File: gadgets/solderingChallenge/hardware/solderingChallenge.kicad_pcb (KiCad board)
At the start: 2 copper layers, 145 x 39 mm, 46 parts, among them J10 USB_A, J12 USB_A, J2 USB_A, J4 USB_A, J6 USB_A, J8 USB_A, U1 LM555xN, U2 LMC555xM, U3 LMC555xMM, U4 LMC555xMM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

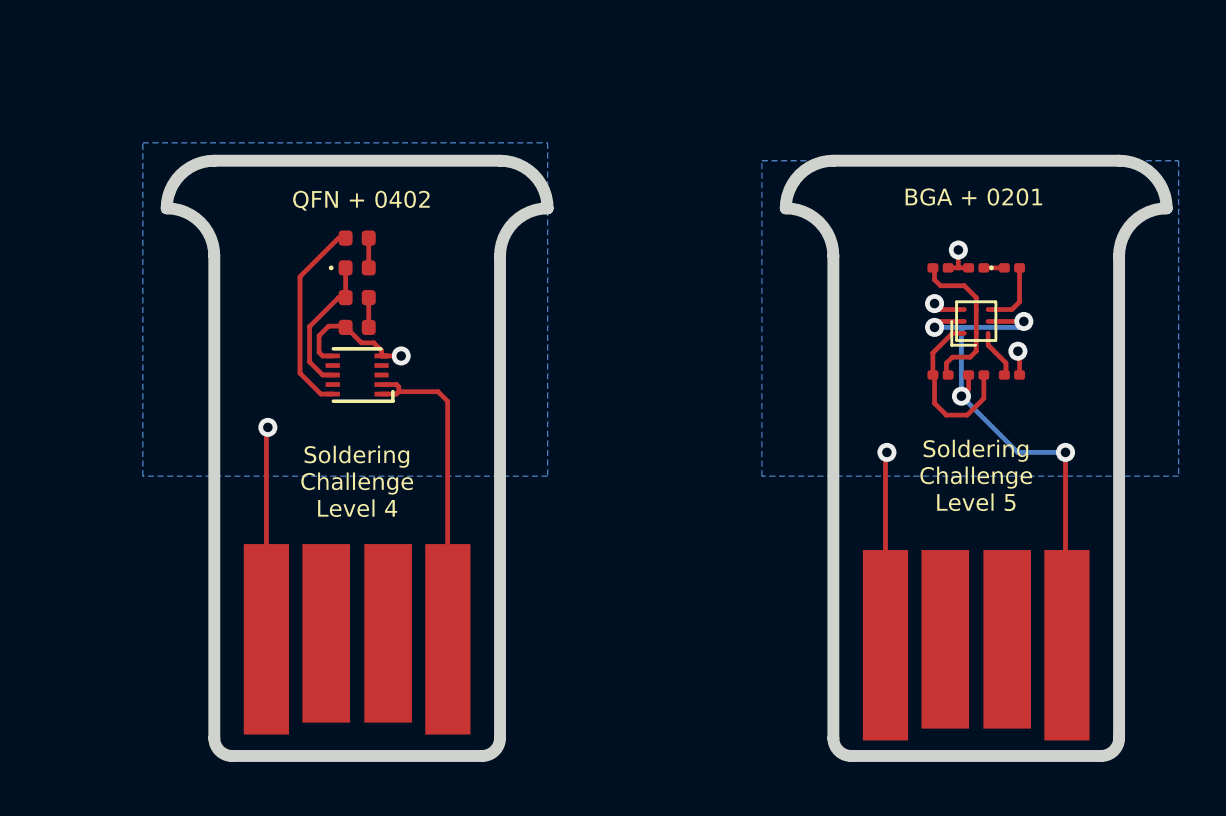
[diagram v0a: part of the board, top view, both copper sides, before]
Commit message: Remove extra level, add documentation
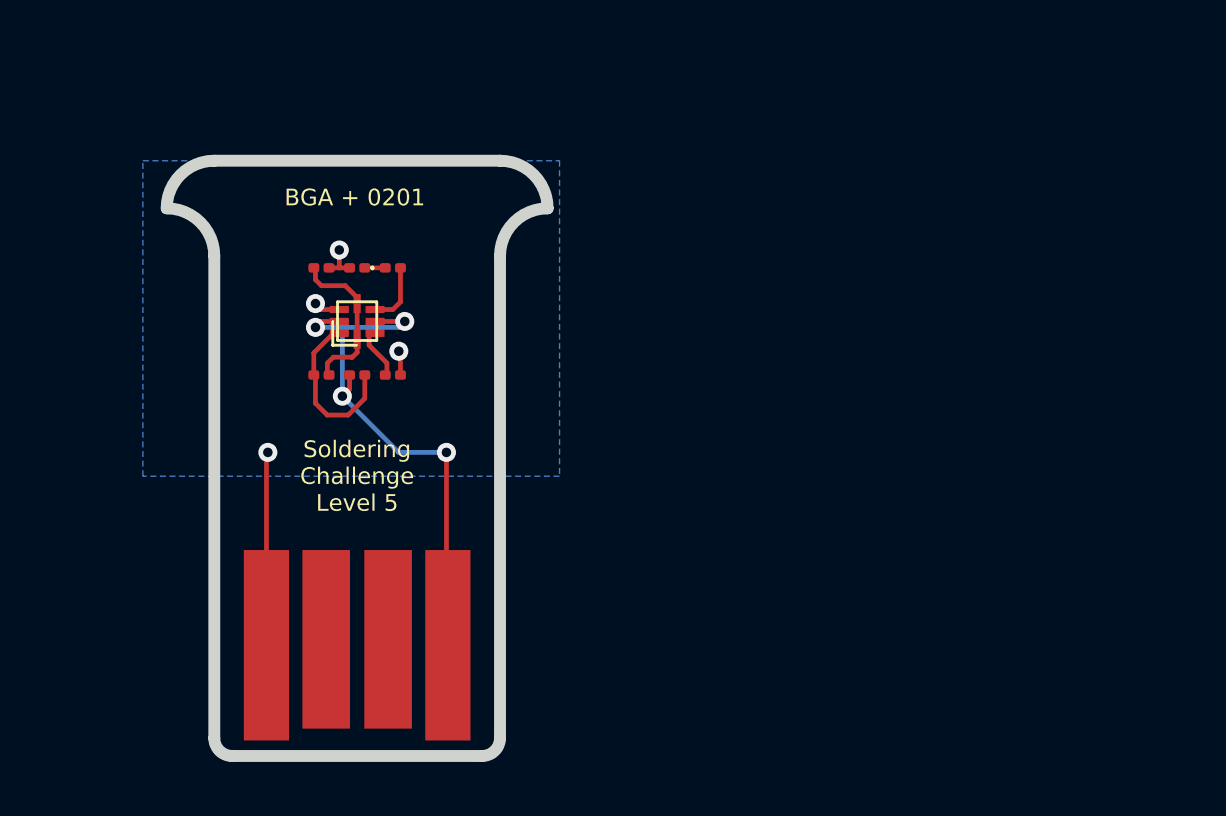
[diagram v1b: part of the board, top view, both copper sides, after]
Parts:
- removed C11: 100n, Capacitor_SMD:C_0402_1005Metric
- removed D6: LED, LED_SMD:LED_0402_1005Metric
- removed J12: USB_A, RoboCamp:usb-PCB
- removed R16: 100k, Resistor_SMD:R_0402_1005Metric
- removed R17: 330R, Resistor_SMD:R_0402_1005Metric
- removed U6: MIC1555-MU, RoboCamp:UTDFN-10
- moved C10 26.0 mm to (190.5, 91.2)
- moved C9 26.0 mm to (193.5, 95.8)
- moved D5 26.0 mm to (193.5, 91.2)
- moved J10 26.0 mm to (192.0, 112.0)
- moved R13 26.0 mm to (192.0, 91.2)
- moved R14 26.0 mm to (192.0, 95.8)
- moved R15 26.0 mm to (190.5, 95.8)
- moved U5 26.0 mm to (192.0, 93.5)
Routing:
- net /Level 4 alternative - 0402/GND: track 14.8 -> 0.00 mm, vias 2 -> 0
- net /Level 4 alternative - 0402/VCC: track 14.0 -> 0.00 mm
- net Net-(R17-Pad2): track 8.38 -> 0.00 mm
- net Net-(C11-Pad2): track 5.98 -> 0.00 mm
- net Net-(D6-Pad2): track 1.21 -> 0.00 mm
- net Net-(C11-Pad1): track 1.21 -> 0.00 mm
- net /Level 5 - 0201/VCC: track 24.3 -> 24.9 mm
- net Net-(C9-Pad1): track 2.06 -> 2.61 mm
- removed copper zone on B.Cu, net /Level 4 alternative - 0402/GND
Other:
- board size 145 x 39 mm -> 119 x 39 mm
- net class Default: clearance 0.2 -> 0.127
- rule trace_clearance: 0.2 -> 0.127
- board text removed: "QFN + 0402"

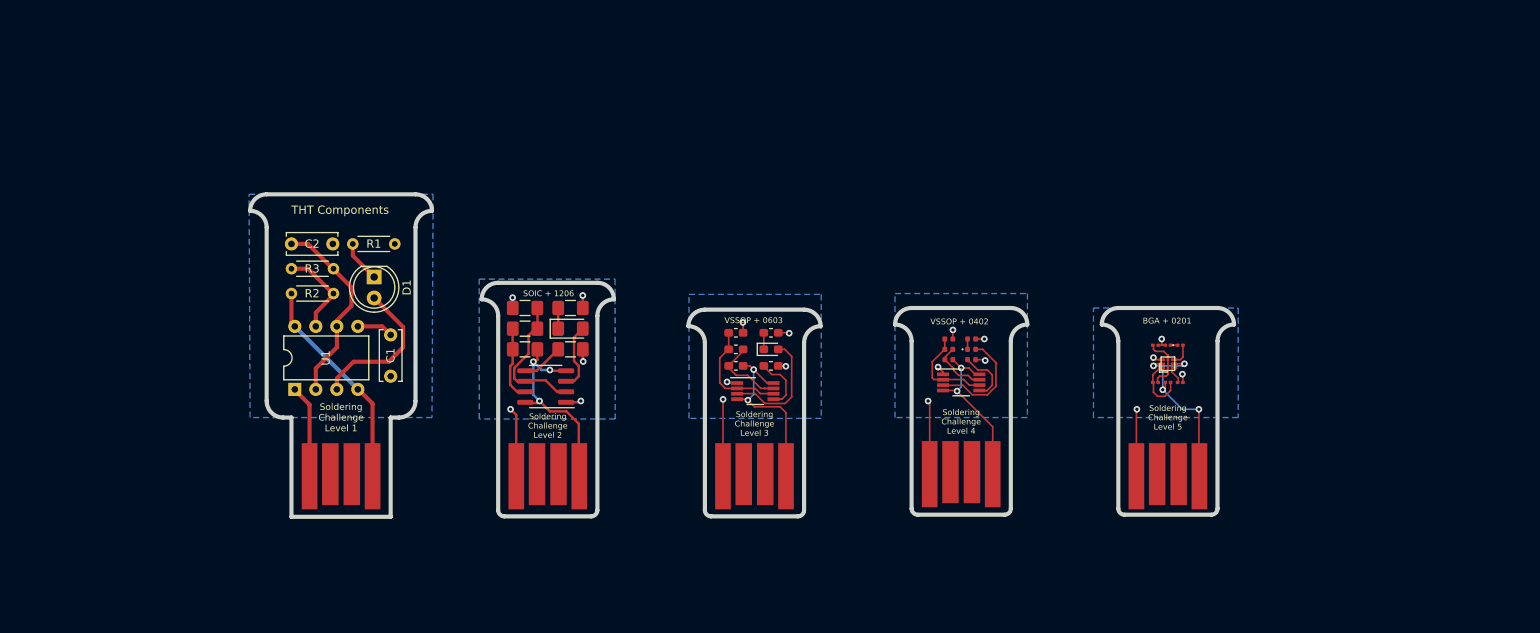
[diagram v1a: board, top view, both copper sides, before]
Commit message: Add L0 to soldering challenge
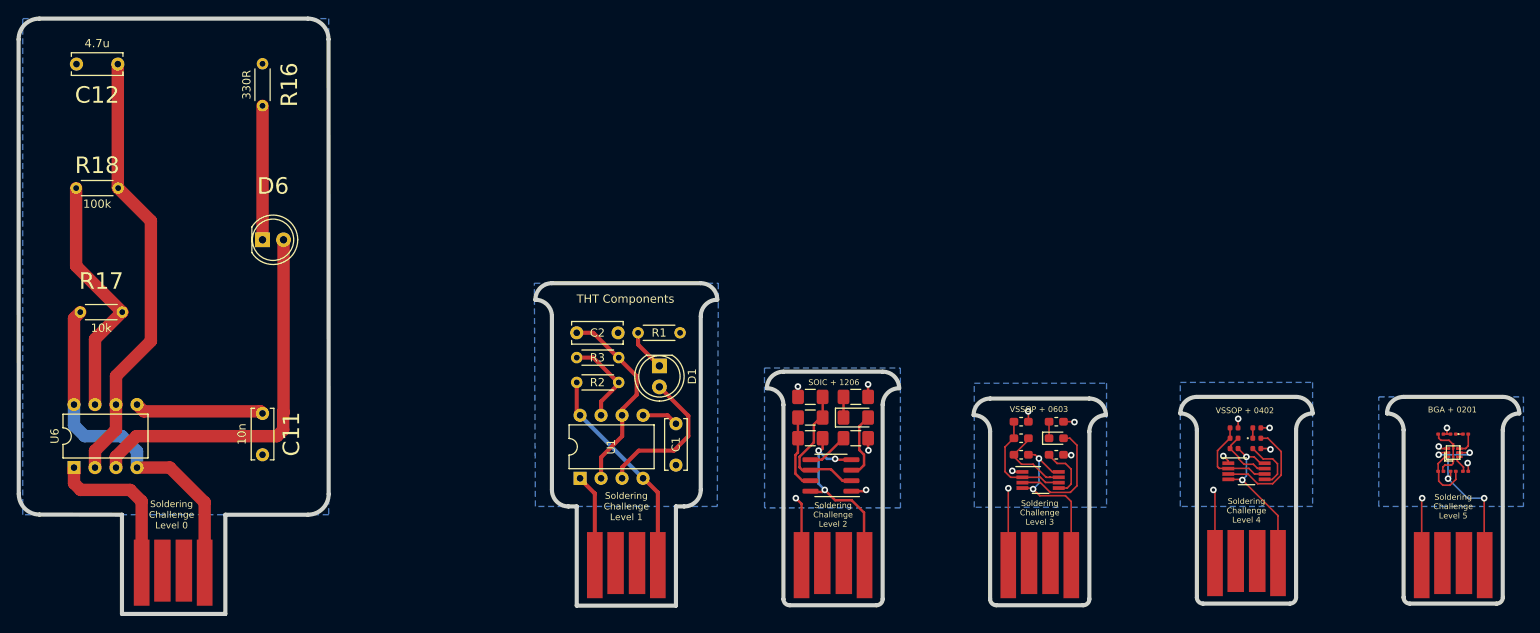
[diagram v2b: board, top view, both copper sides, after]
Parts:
- added B0: Board, kikit:Board, F.Cu at (60.0, 51.8)
- added B1: Board, kikit:Board, F.Cu at (126.8, 83.8)
- added B2: Board, kikit:Board, F.Cu at (151.8, 94.5)
- added B3: Board, kikit:Board, F.Cu at (176.5, 97.8)
- added B4: Board, kikit:Board, F.Cu at (201.8, 97.5)
- added B5: Board, kikit:Board, F.Cu at (226.8, 97.5)
- added C11: 10n, Capacitor_THT:C_Disc_D6.0mm_W2.5mm_P5.00mm, F.Cu at (82.5, 99.5)
- added C12: 4.7u, Capacitor_THT:C_Disc_D6.0mm_W2.5mm_P5.00mm, F.Cu at (65.0, 57.2)
- added D6: LED, LED_THT:LED_D5.0mm, F.Cu at (82.5, 78.5)
- added J1: USB_A, RoboCamp:usb-PCB, F.Cu at (71.7, 123.7)
- added R16: 330R, Resistor_THT:R_Axial_DIN0204_L3.6mm_D1.6mm_P5.08mm_Horizontal, F.Cu at (82.5, 57.2)
- added R17: 10k, Resistor_THT:R_Axial_DIN0204_L3.6mm_D1.6mm_P5.08mm_Horizontal, F.Cu at (60.5, 87.2)
- added R18: 100k, Resistor_THT:R_Axial_DIN0204_L3.6mm_D1.6mm_P5.08mm_Horizontal, F.Cu at (60.0, 72.2)
- added U6: LM555xN, Package_DIP:DIP-8_W7.62mm, F.Cu at (59.7, 106.0)
- moved C1 36.1 mm to (132.5, 100.8)
- moved C10 36.1 mm to (225.0, 102.0)
- moved C2 36.1 mm to (120.5, 89.8)
- moved C3 36.1 mm to (154.2, 102.5)
- moved C4 36.1 mm to (148.8, 97.5)
- moved C5 36.1 mm to (178.5, 104.5)
- moved C6 36.1 mm to (174.2, 100.5)
- moved C7 36.1 mm to (202.8, 103.8)
- moved C8 36.1 mm to (200.0, 101.2)
- moved C9 36.1 mm to (228.0, 106.5)
- moved D1 36.1 mm to (130.5, 93.8)
- moved D2 36.1 mm to (154.2, 100.0)
- moved D3 36.1 mm to (178.5, 102.5)
- moved D4 36.1 mm to (202.8, 102.5)
- moved D5 36.1 mm to (228.0, 102.0)
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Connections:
- J10 pad 2: (no net) -> unconnected-(J10-Pad2)
- J10 pad 3: (no net) -> unconnected-(J10-Pad3)
- J2 pad 2: (no net) -> unconnected-(J2-Pad2)
- J2 pad 3: (no net) -> unconnected-(J2-Pad3)
- J4 pad 2: (no net) -> unconnected-(J4-Pad2)
- J4 pad 3: (no net) -> unconnected-(J4-Pad3)
- J6 pad 2: (no net) -> unconnected-(J6-Pad2)
- J6 pad 3: (no net) -> unconnected-(J6-Pad3)
- J8 pad 2: (no net) -> unconnected-(J8-Pad2)
- J8 pad 3: (no net) -> unconnected-(J8-Pad3)
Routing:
- net Net-(C12-Pad1): track 0.00 -> 53.3 mm
- net Net-(D6-Pad2): track 0.00 -> 45.9 mm
- net /Level 0 - THT/VCC: track 0.00 -> 43.3 mm
- net Net-(R17-Pad2): track 0.00 -> 29.9 mm
- net /Level 0 - THT/GND: track 0.00 -> 19.6 mm
- net Net-(D6-Pad1): track 0.00 -> 16.2 mm
- net Net-(C11-Pad1): track 0.00 -> 15.6 mm
- added copper zone on B.Cu, net /Level 0 - THT/GND
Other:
- board size 119 x 39 mm -> 181.5 x 72 mm
- net class Default removed
- board text added: "Soldering Challenge Level 0"
